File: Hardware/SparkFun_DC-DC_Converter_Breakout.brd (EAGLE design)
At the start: 27.9 x 27.9 mm, 14 parts, among them Q1 MOSFET-NCHANNELSMD, U1 DC-DC_CONVERTER

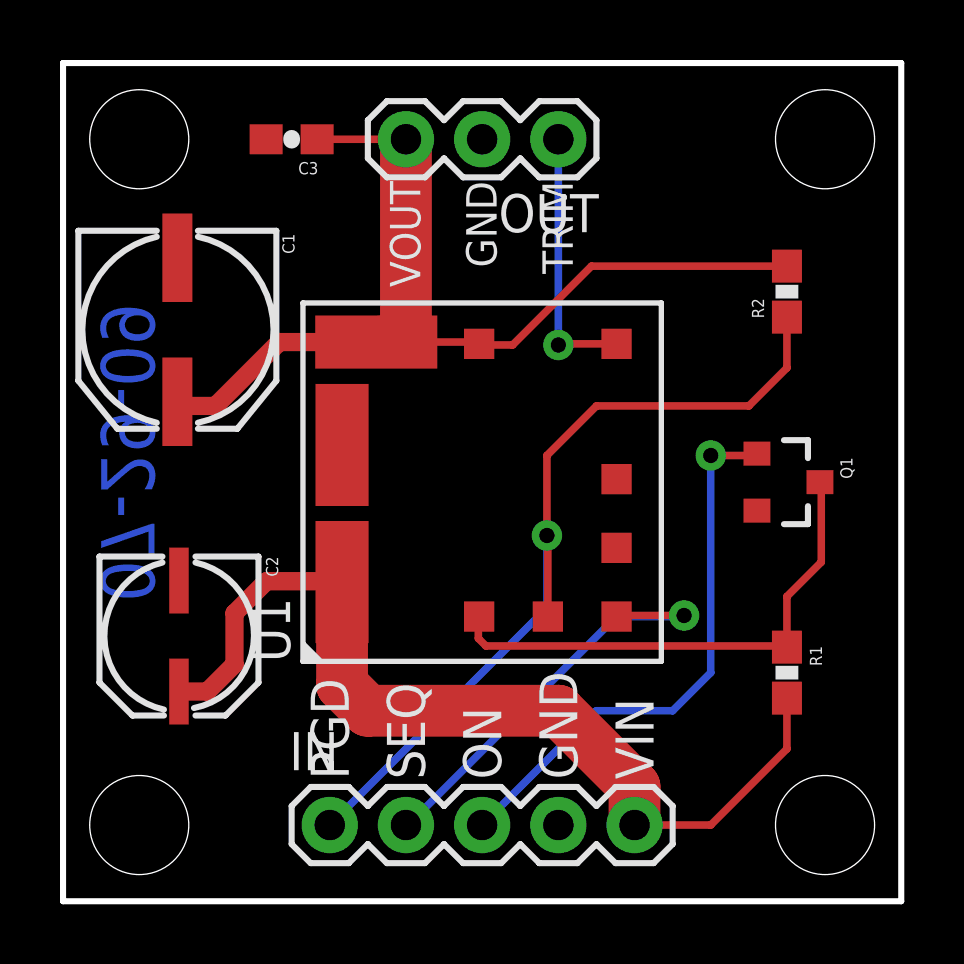
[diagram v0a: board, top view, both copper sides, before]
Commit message: added local fiducials
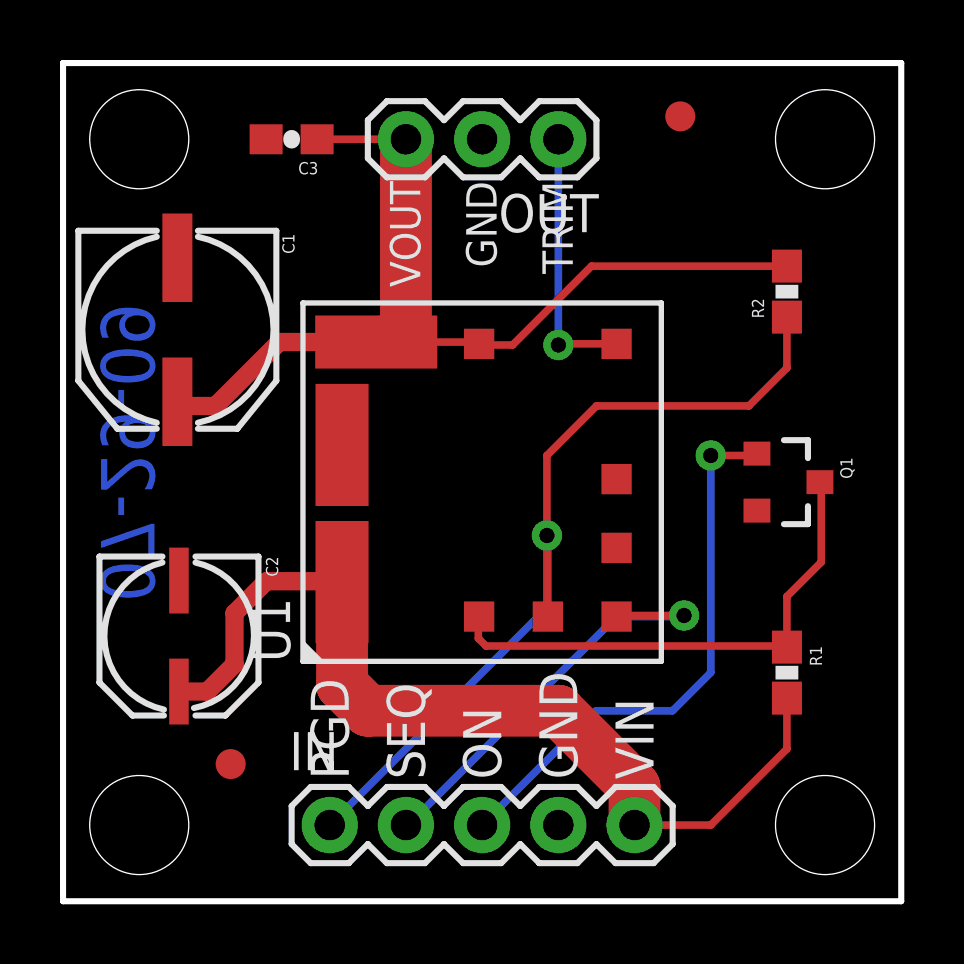
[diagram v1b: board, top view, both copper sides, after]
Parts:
- added FID1, FID2: FIDUCIAL1X2, SparkFun-Aesthetics:FIDUCIAL-1X2
